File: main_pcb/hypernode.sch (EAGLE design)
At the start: 30 parts, among them IC1 74HCT245D, U1 MAX488, X2 JST-XH-CONNECTOR-02-PIN, X4 JST-XH-CONNECTOR-02-PIN, X7 JST-XH-03-PIN-LONG-PAD, X8 JST-XH-03-PIN-LONG-PAD

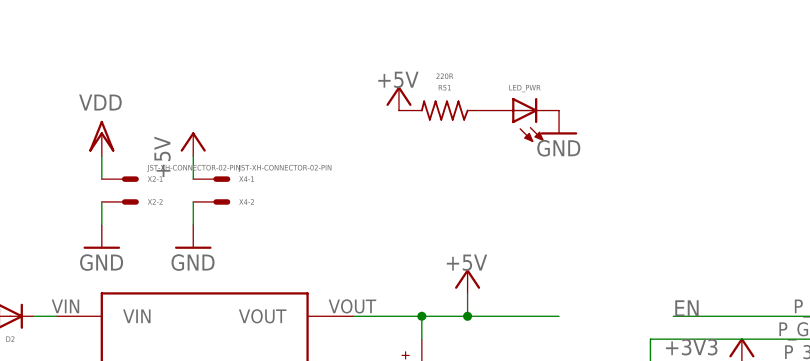
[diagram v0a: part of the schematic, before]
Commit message: feed power led from 3v3
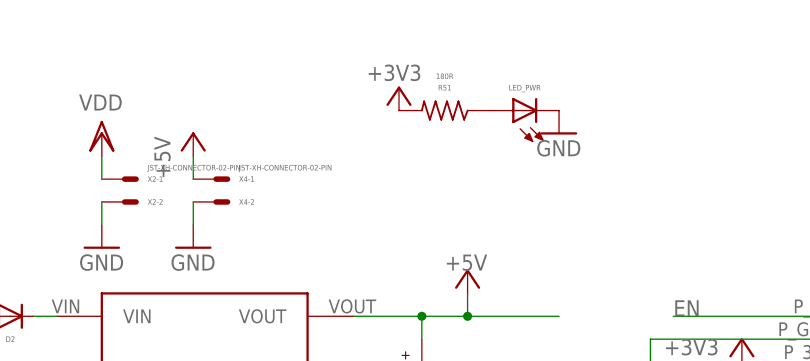
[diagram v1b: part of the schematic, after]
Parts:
- R51: value 220R -> 180R
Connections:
- net +3V3: now also R51.2
- net +5V: no longer R51.2
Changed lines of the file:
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@@
 <part name="GND6" library="supply1" library_urn="urn:adsk.eagle:library:371" deviceset="GND" device=""/>
 <part name="D2" library="Multischriever" deviceset="DIODE_SMB" device=""/>
-<part name="R51" library="Multischriever" deviceset="RESISTOR" device="" value="220R"/>
+<part name="R51" library="Multischriever" deviceset="RESISTOR" device="" value="180R"/>
 <part name="GND28" library="supply1" library_urn="urn:adsk.eagle:library:371" deviceset="GND" device=""/>
 <part name="LED_PWR" library="Multischriever" deviceset="LED" device="0603"/>
-<part name="P+4" library="supply1" library_urn="urn:adsk.eagle:library:371" deviceset="+5V" device=""/>
 <part name="U$15" library="SparkFun-Connectors" deviceset="RJ45-8" device="PTH"/>
 <part name="GND36" library="supply1" library_urn="urn:adsk.eagle:library:371" deviceset="GND" device=""/>
@@
 <part name="R5" library="Multischriever" deviceset="RESISTOR" device="" value="100R"/>
 <part name="R8" library="Multischriever" deviceset="RESISTOR" device="" value="100R"/>
+<part name="+3V2" library="supply1" library_urn="urn:adsk.eagle:library:371" deviceset="+3V3" device=""/>
 </parts>
 <sheets>
@@
 <attribute name="VALUE" x="41.91" y="100.33" size="0.6096" layer="96" rot="R180" align="center"/>
 </instance>
-<instance part="P+4" gate="1" x="27.94" y="99.06" smashed="yes">
-<attribute name="VALUE" x="25.4" y="99.06" size="1.778" layer="96"/>
-</instance>
 <instance part="U$15" gate="G$1" x="228.6" y="-50.8" smashed="yes">
 <attribute name="NAME" x="220.98" y="-37.592" size="1.778" layer="95"/>
@@
 <attribute name="NAME" x="5.08" y="5.08" size="0.6096" layer="95" rot="R180" align="center"/>
 <attribute name="VALUE" x="5.08" y="6.35" size="0.6096" layer="96" rot="R180" align="center"/>
+</instance>
+<instance part="+3V2" gate="G$1" x="27.94" y="99.06" smashed="yes">
+<attribute name="VALUE" x="30.48" y="101.6" size="1.778" layer="96" rot="R180"/>
 </instance>
 </instances>
@@
 </segment>
 <segment>
-<pinref part="R51" gate="G$1" pin="2"/>
-<pinref part="P+4" gate="1" pin="+5V"/>
-</segment>
-<segment>
 <pinref part="X4" gate="-1" pin="S"/>
 <wire x1="5.08" y1="88.9" x2="5.08" y2="91.44" width="0.1524" layer="91"/>
@@
 <wire x1="5.08" y1="7.62" x2="5.08" y2="10.16" width="0.1524" layer="91"/>
 </segment>
-</net>
+<segment>
+<pinref part="R51" gate="G$1" pin="2"/>
+<pinref part="+3V2" gate="G$1" pin="+3V3"/>
+</segment>
+</net>
